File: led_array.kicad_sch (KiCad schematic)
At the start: 128 parts

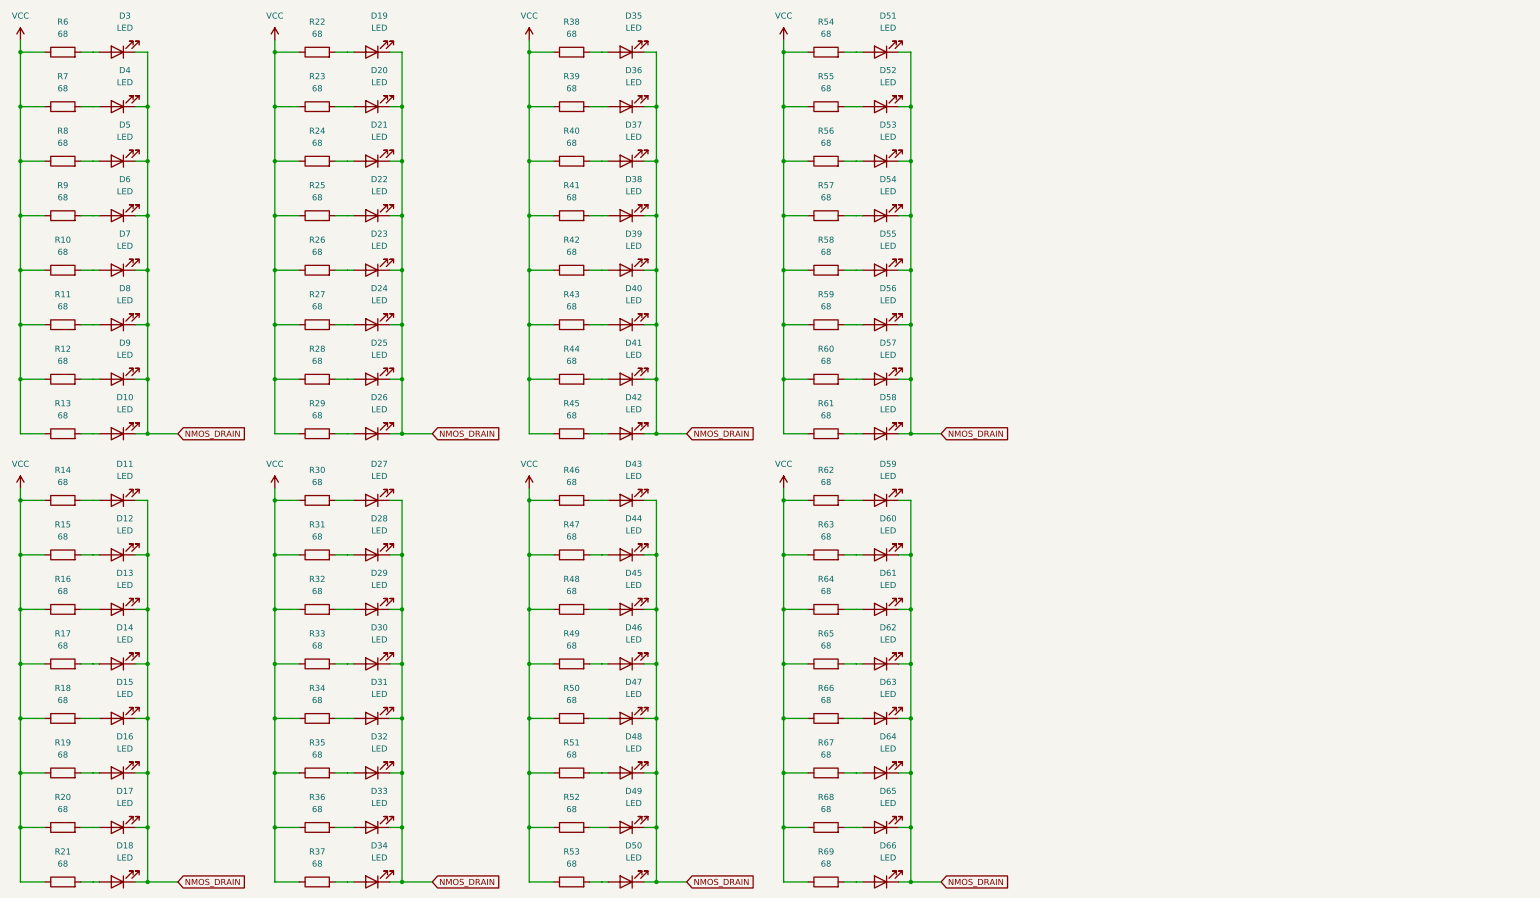
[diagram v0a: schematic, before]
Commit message: Draft version for 96 well plate
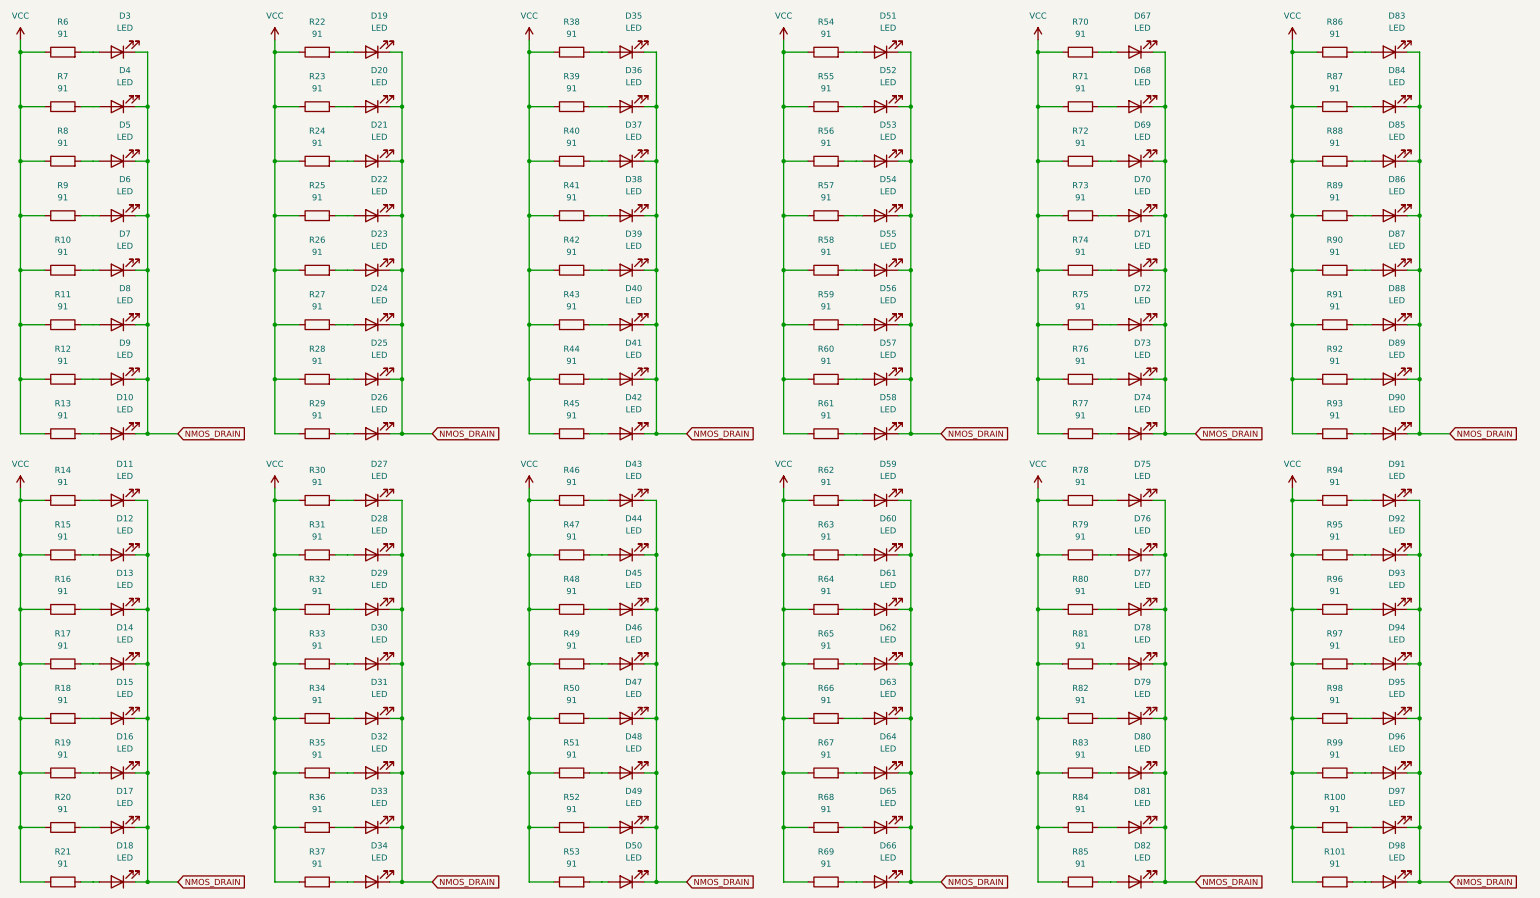
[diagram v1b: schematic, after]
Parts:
- added D67, D68, D69, D70, D71, D72, D73, D74, D75, D76, D77, D78, D79, D80, D81, D82, D83, D84, D85, D86, D87, D88, D89, D90, D91, D92, D93, D94, D95, D96, D97, D98: LED, LED_SMD:LED_0603_1608Metric, symbol Device:LED
- added R100, R101, R70, R71, R72, R73, R74, R75, R76, R77, R78, R79, R80, R81, R82, R83, R84, R85, R86, R87, R88, R89, R90, R91, R92, R93, R94, R95, R96, R97, R98, R99: 91, Resistor_SMD:R_0603_1608Metric, symbol Device:R
- R10, R11, R12, R13, R14, R15, R16, R17, R18, R19, R20, R21, R22, R23, R24, R25, R26, R27, R28, R29, R30, R31, R32, R33, R34, R35, R36, R37, R38, R39, R40, R41, R42, R43, R44, R45, R46, R47, R48, R49, R50, R51, R52, R53, R54, R55, R56, R57, R58, R59, R6, R60, R61, R62, R63, R64, R65, R66, R67, R68, R69, R7, R8, R9: value 68 -> 91
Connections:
- net NMOS_DRAIN: now also D67.1 (K), D68.1 (K), D69.1 (K), D70.1 (K), D71.1 (K), D72.1 (K), D73.1 (K), D74.1 (K), D75.1 (K), D76.1 (K), D77.1 (K), D78.1 (K), D79.1 (K), D80.1 (K), D81.1 (K), D82.1 (K), D83.1 (K), D84.1 (K), D85.1 (K), D86.1 (K), D87.1 (K), D88.1 (K), D89.1 (K), D90.1 (K), D91.1 (K), D92.1 (K), D93.1 (K), D94.1 (K), D95.1 (K), D96.1 (K), D97.1 (K), D98.1 (K)
- net VCC: now also R100.1, R101.1, R70.1, R71.1, R72.1, R73.1, R74.1, R75.1, R76.1, R77.1, R78.1, R79.1, R80.1, R81.1, R82.1, R83.1, R84.1, R85.1, R86.1, R87.1, R88.1, R89.1, R90.1, R91.1, R92.1, R93.1, R94.1, R95.1, R96.1, R97.1, R98.1, R99.1
- new net: D80.2 (A), R83.2
- new net: D79.2 (A), R82.2
- new net: D86.2 (A), R89.2
- new net: D67.2 (A), R70.2
- new net: D73.2 (A), R76.2
- new net: D77.2 (A), R80.2
- new net: D70.2 (A), R73.2
- new net: D88.2 (A), R91.2
- new net: D87.2 (A), R90.2
- new net: D72.2 (A), R75.2
- new net: D97.2 (A), R100.2
- new net: D91.2 (A), R94.2
- new net: D92.2 (A), R95.2
- new net: D94.2 (A), R97.2
- new net: D90.2 (A), R93.2
- new net: D96.2 (A), R99.2
- new net: D75.2 (A), R78.2
- new net: D95.2 (A), R98.2
- new net: D93.2 (A), R96.2
- new net: D84.2 (A), R87.2
- new net: D68.2 (A), R71.2
- new net: D69.2 (A), R72.2
- new net: D89.2 (A), R92.2
- new net: D74.2 (A), R77.2
- new net: D85.2 (A), R88.2
- new net: D98.2 (A), R101.2
- new net: D81.2 (A), R84.2
- new net: D76.2 (A), R79.2
- new net: D83.2 (A), R86.2
- new net: D71.2 (A), R74.2
- new net: D78.2 (A), R81.2
- new net: D82.2 (A), R85.2

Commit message: update USB-C conn and add JLC PNs
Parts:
- D10, D11, D12, D13, D14, D15, D16, D17, D18, D19, D20, D21, D22, D23, D24, D25, D26, D27, D28, D29, D3, D30, D31, D32, D33, D34, D35, D36, D37, D38, D39, D4, D40, D41, D42, D43, D44, D45, D46, D47, D48, D49, D5, D50, D51, D52, D53, D54, D55, D56, D57, D58, D59, D6, D60, D61, D62, D63, D64, D65, D66, D67, D68, D69, D7, D70, D71, D72, D73, D74, D75, D76, D77, D78, D79, D8, D80, D81, D82, D83, D84, D85, D86, D87, D88, D89, D9, D90, D91, D92, D93, D94, D95, D96, D97, D98: DigiKey C503B-BAN-CZ0A0452CT-ND -> (none); JLC (none) -> C5875724; Mouser 941-C503BBANCZ0A0452 -> (none)
- R10, R100, R101, R11, R12, R13, R14, R15, R16, R17, R18, R19, R20, R21, R22, R23, R24, R25, R26, R27, R28, R29, R30, R31, R32, R33, R34, R35, R36, R37, R38, R39, R40, R41, R42, R43, R44, R45, R46, R47, R48, R49, R50, R51, R52, R53, R54, R55, R56, R57, R58, R59, R6, R60, R61, R62, R63, R64, R65, R66, R67, R68, R69, R7, R70, R71, R72, R73, R74, R75, R76, R77, R78, R79, R8, R80, R81, R82, R83, R84, R85, R86, R87, R88, R89, R9, R90, R91, R92, R93, R94, R95, R96, R97, R98, R99: JLC (none) -> C22775

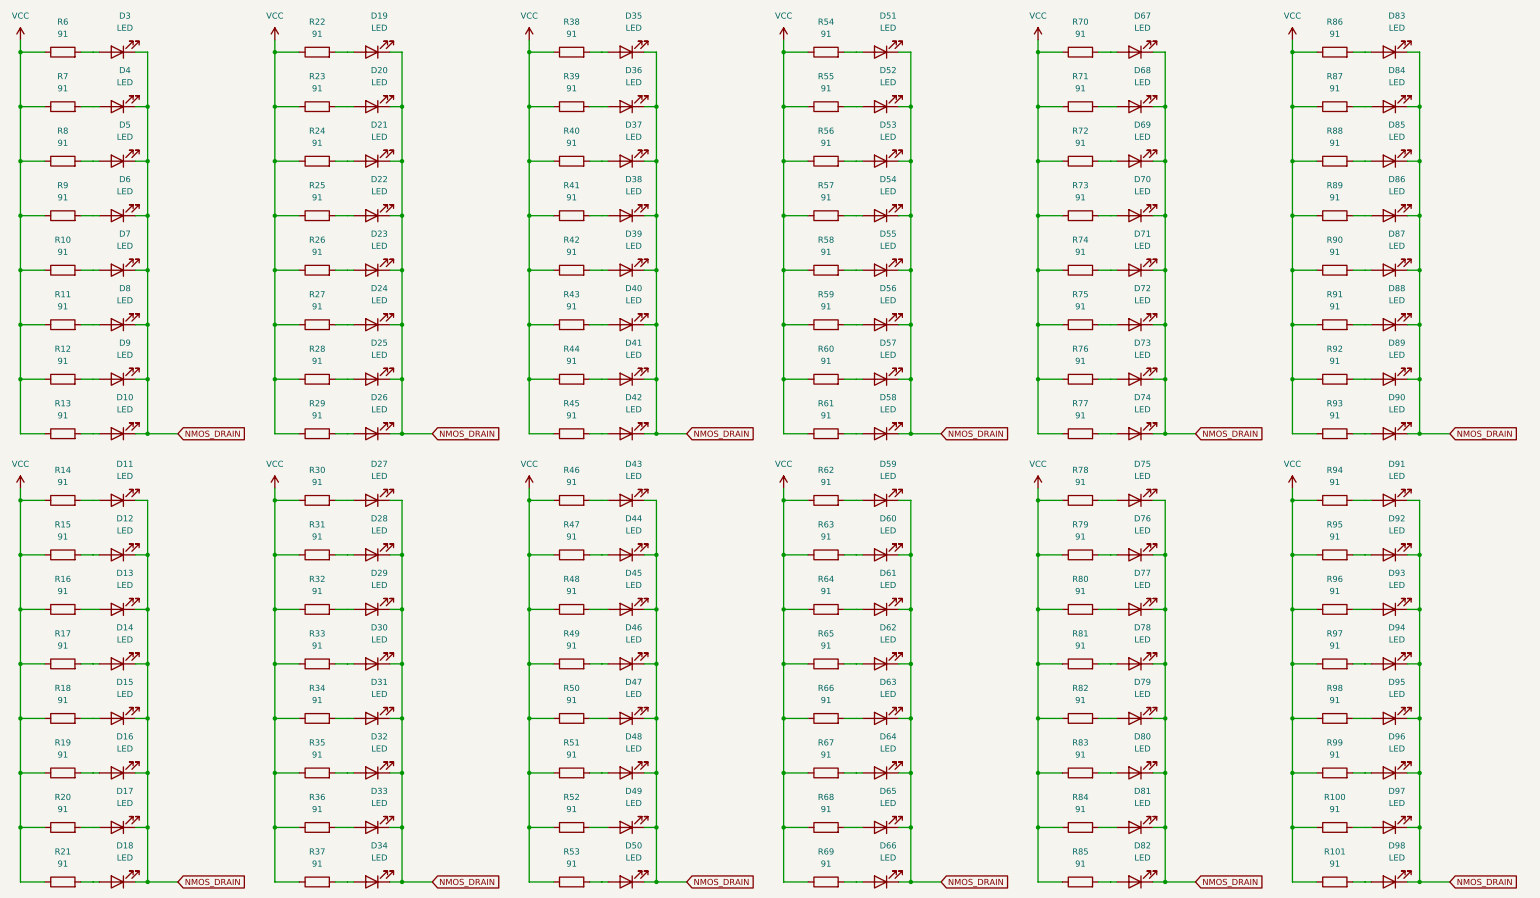
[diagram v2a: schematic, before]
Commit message: Add DigiKey and Mouser PNs. Update manf outputs
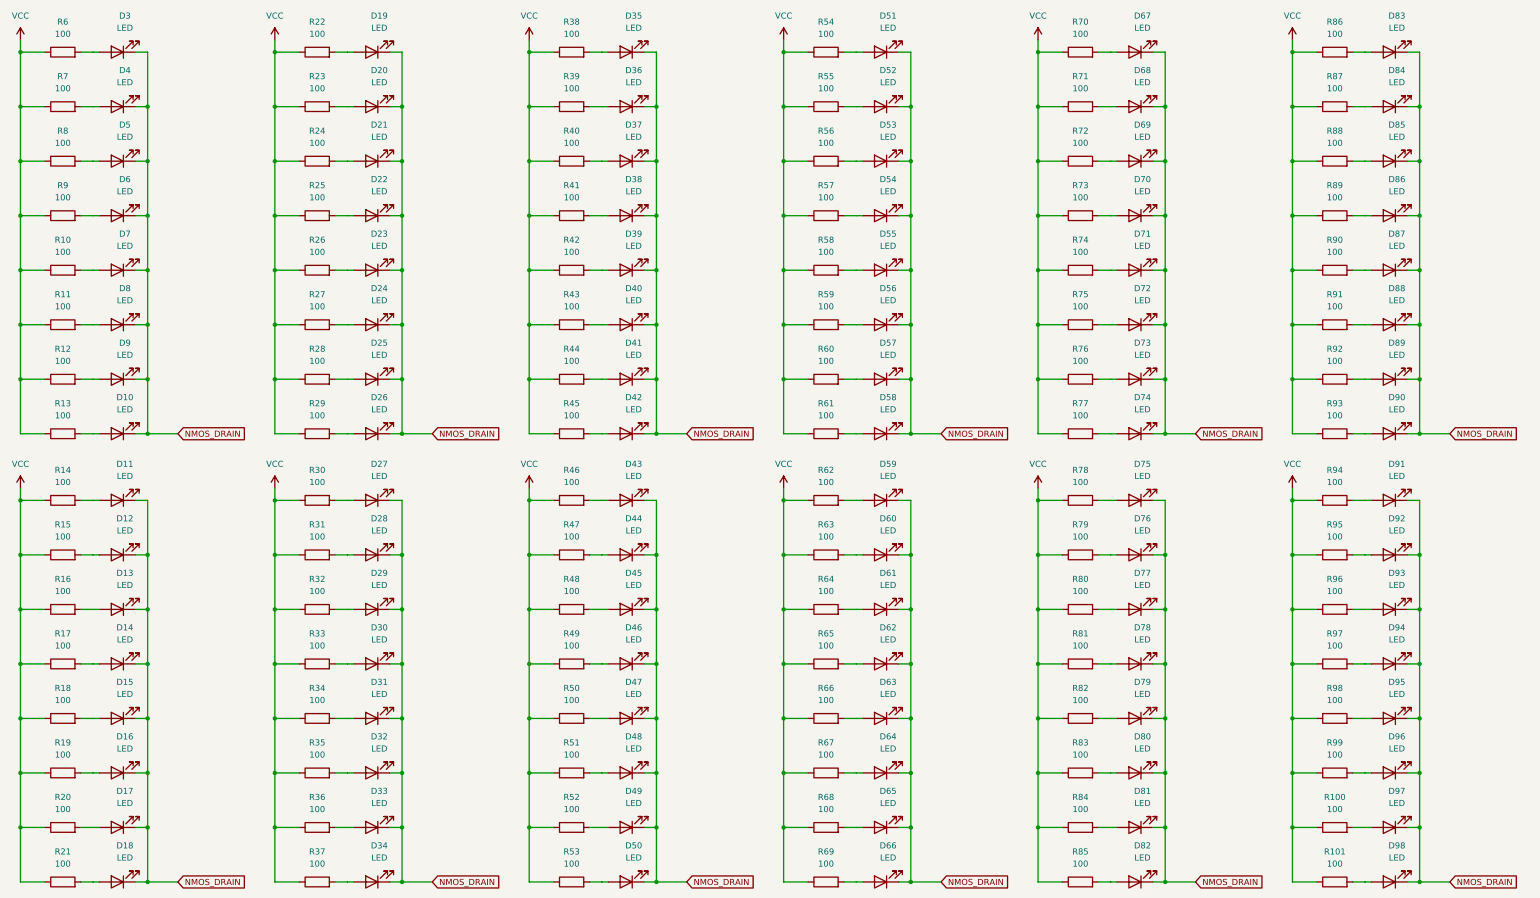
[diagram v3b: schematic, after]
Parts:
- D10, D11, D12, D13, D14, D15, D16, D17, D18, D19, D20, D21, D22, D23, D24, D25, D26, D27, D28, D29, D3, D30, D31, D32, D33, D34, D35, D36, D37, D38, D39, D4, D40, D41, D42, D43, D44, D45, D46, D47, D48, D49, D5, D50, D51, D52, D53, D54, D55, D56, D57, D58, D59, D6, D60, D61, D62, D63, D64, D65, D66, D67, D68, D69, D7, D70, D71, D72, D73, D74, D75, D76, D77, D78, D79, D8, D80, D81, D82, D83, D84, D85, D86, D87, D88, D89, D9, D90, D91, D92, D93, D94, D95, D96, D97, D98: DigiKey (none) -> 754-1434-1-ND; Mouser (none) -> 604-APT1608QBC/D
- R10, R100, R101, R11, R12, R13, R14, R15, R16, R17, R18, R19, R20, R21, R22, R23, R24, R25, R26, R27, R28, R29, R30, R31, R32, R33, R34, R35, R36, R37, R38, R39, R40, R41, R42, R43, R44, R45, R46, R47, R48, R49, R50, R51, R52, R53, R54, R55, R56, R57, R58, R59, R6, R60, R61, R62, R63, R64, R65, R66, R67, R68, R69, R7, R70, R71, R72, R73, R74, R75, R76, R77, R78, R79, R8, R80, R81, R82, R83, R84, R85, R86, R87, R88, R89, R9, R90, R91, R92, R93, R94, R95, R96, R97, R98, R99: value 91 -> 100; DigiKey 311-68ARCT-ND -> (none); Mouser 603-RC0805JR-0768RL -> (none)
